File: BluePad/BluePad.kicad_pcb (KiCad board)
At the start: 2 copper layers, 76.2 x 95.2 mm, 213 parts, among them J1 USB_OTG, SW1 SW_RST, U1 ATMEGA32U4RC-A, U2 IS31FL3731, X1 16Mhz

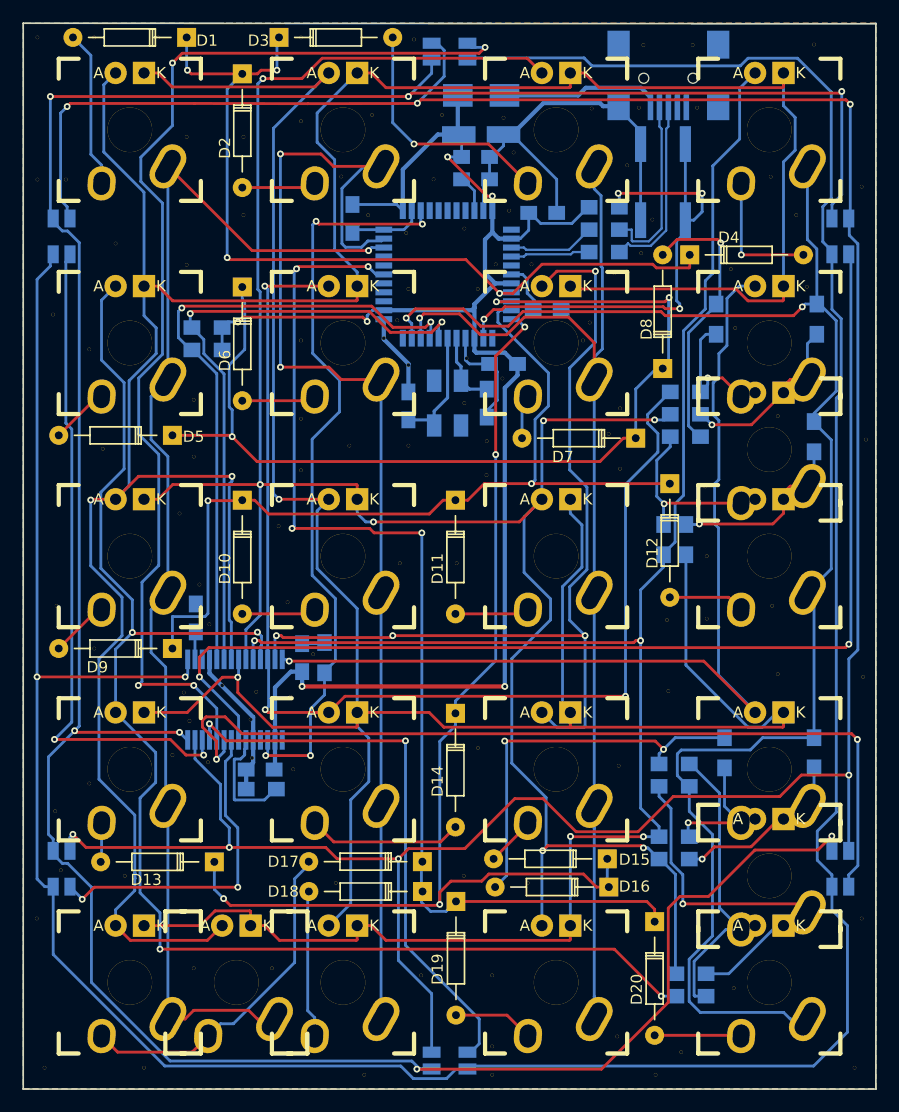
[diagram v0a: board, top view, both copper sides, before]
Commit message: Renamed BlueWeevil to LFK78
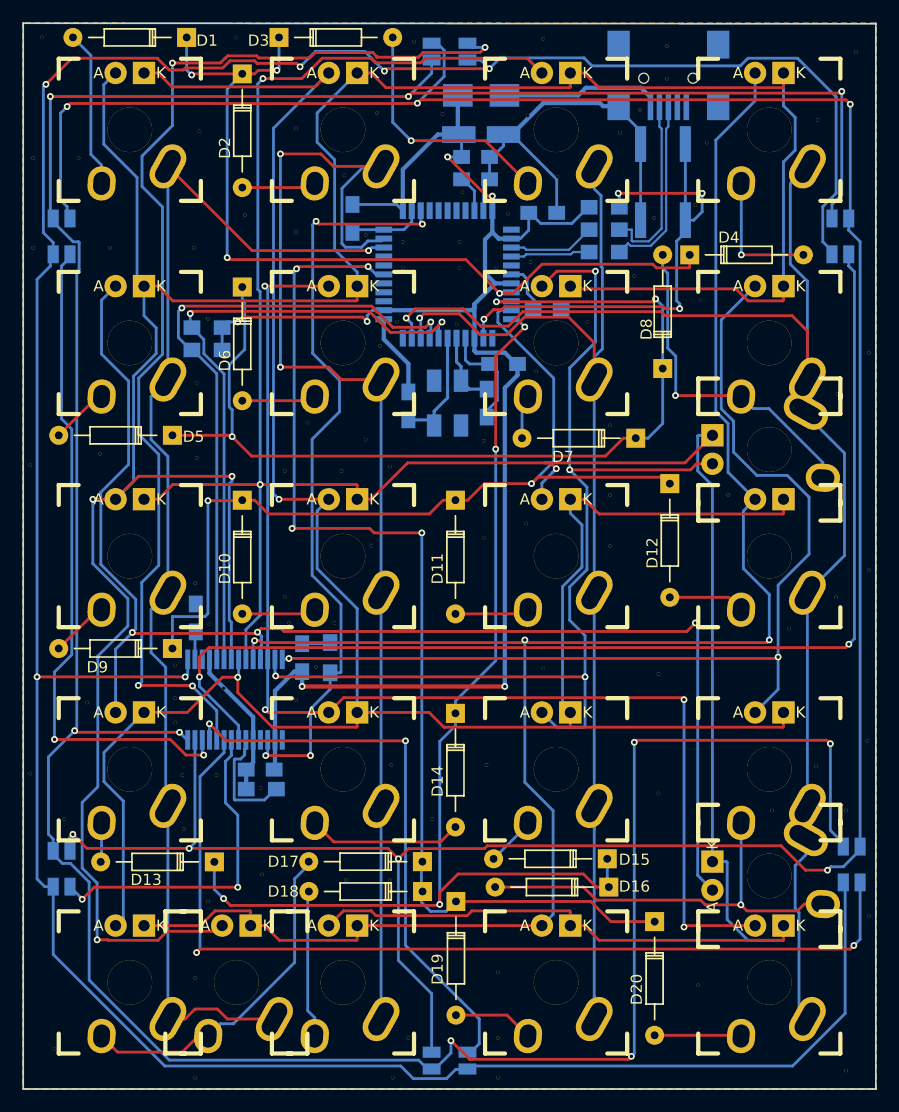
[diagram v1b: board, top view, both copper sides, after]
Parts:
- removed JP_ENTER_1, JP_ENTER_2, JP_ENTER_3, JP_ENTER_4, JP_PLUS_1, JP_PLUS_2, JP_PLUS_3, JP_PLUS_4: Jumper_NC_Small, Resistors_SMD:R_0805_HandSoldering
- removed JP_SW12_1, JP_SW12_2, JP_SW16_1, JP_SW16_2, JP_SW20_1, JP_SW20_2, JP_SW8_1, JP_SW8_2: Jumper_NO_Small, Resistors_SMD:R_0805_HandSoldering
- removed the REF** at (91.8, 41.0)
- removed the REF** at (34.5, 48.2)
- removed the REF** at (81.4, 41.4)
- removed the REF** at (72.4, 30.6)
- removed the REF** at (72.0, 35.8)
- removed the REF** at (60.8, 47.2)
- removed the REF** at (70.0, 56.4)
- removed the REF** at (68.0, 53.0)
- removed the REF** at (68.2, 49.0)
- removed the REF** at (71.4, 50.8)
- removed the REF** at (78.6, 47.4)
- removed the REF** at (69.2, 42.8)
- removed the REF** at (35.7, 57.1)
- removed the REF** at (63.0, 42.8)
- removed the REF** at (59.4, 36.2)
- removed the REF** at (62.8, 37.8)
- removed the REF** at (68.0, 37.4)
- removed the REF** at (79.2, 45.8)
- removed the REF** at (74.0, 40.6)
- removed the REF** at (63.0, 56.8)
- removed the REF** at (63.0, 49.6)
- removed the REF** at (53.4, 54.4)
- removed the REF** at (53.4, 59.0)
- removed the REF** at (31.2, 45.1)
- removed the REF** at (51.4, 64.0)
- removed the REF** at (52.2, 70.8)
- removed the REF** at (49.4, 78.8)
- removed the REF** at (42.9, 78.9)
- removed the REF** at (31.4, 89.5)
- removed the REF** at (81.8, 85.4)
- removed the REF** at (92.1, 105.3)
- removed the REF** at (87.4, 111.0)
- removed the REF** at (81.7, 109.6)
- removed the REF** at (98.6, 42.6)
- removed the REF** at (92.2, 46.3)
- removed the REF** at (95.4, 32.8)
- removed the REF** at (96.0, 54.2)
- removed the REF** at (89.5, 60.5)
- removed the REF** at (89.7, 66.7)
- removed the REF** at (89.7, 72.3)
- removed the REF** at (86.1, 72.4)
- removed the REF** at (95.5, 71.1)
- removed the REF** at (96.0, 77.2)
- removed the REF** at (86.2, 78.7)
- removed the REF** at (54.5, 75.4)
- removed the REF** at (52.5, 79.2)
- removed the REF** at (97.7, 36.2)
- removed the REF** at (45.2, 72.8)
- removed the REF** at (44.3, 69.2)
- removed the REF** at (49.0, 84.7)
- removed the REF** at (46.4, 78.2)
- removed the REF** at (43.4, 81.4)
- removed the REF** at (103.6, 77.5)
- removed the REF** at (103.9, 56.3)
- removed the REF** at (80.9, 55.8)
- removed the REF** at (81.9, 53.5)
- removed the REF** at (63.5, 20.5)
- removed the REF** at (43.8, 57.8)
- removed the REF** at (71.5, 27.5)
- removed the REF** at (65.2, 33.0)
- removed the REF** at (66.0, 27.2)
- removed the REF** at (57.0, 32.8)
- removed the REF** at (59.8, 27.2)
- removed the REF** at (82.5, 31.8)
- removed the REF** at (79.4, 26.7)
- removed the REF** at (53.4, 20.3)
- removed the REF** at (99.2, 21.0)
- removed the REF** at (103.5, 33.7)
- removed the REF** at (81.9, 58.9)
- removed the REF** at (103.5, 99.1)
- removed the REF** at (102.9, 112.4)
- removed the REF** at (85.1, 113.0)
- removed the REF** at (56.5, 95.9)
- removed the REF** at (50.8, 103.5)
- removed the REF** at (43.8, 103.5)
- removed the REF** at (48.9, 81.3)
- removed the REF** at (52.7, 85.7)
- removed the REF** at (41.9, 84.5)
- removed the REF** at (34.9, 74.9)
- removed the REF** at (70.0, 59.4)
- removed the REF** at (34.5, 87.0)
- removed the REF** at (37.7, 95.2)
- removed the REF** at (44.5, 90.8)
- removed the REF** at (45.1, 85.1)
- removed the REF** at (62.2, 67.3)
- removed the REF** at (67.3, 67.3)
- removed the REF** at (42.5, 62.9)
- removed the REF** at (43.8, 52.7)
- removed the REF** at (31.6, 71.1)
- removed the REF** at (36.8, 38.7)
- removed the REF** at (63.0, 60.3)
- removed the REF** at (48.3, 36.2)
- removed the REF** at (43.2, 40.6)
- removed the REF** at (48.3, 29.2)
- removed the REF** at (43.2, 29.2)
- removed the REF** at (40.6, 20.3)
- removed the REF** at (34.9, 20.3)
- removed the REF** at (32.4, 33.0)
- removed the REF** at (29.8, 33.0)
- removed the REF** at (29.8, 20.3)
- removed the REF** at (73.7, 95.9)
- removed the REF** at (31.9, 94.7)
- removed the REF** at (67.9, 95.2)
- removed the REF** at (69.2, 83.8)
- removed the REF** at (70.5, 104.1)
- removed the REF** at (64.1, 104.1)
- removed the REF** at (70.5, 110.5)
- removed the REF** at (70.5, 113.0)
- removed the REF** at (59.1, 113.0)
- removed the REF** at (39.4, 112.4)
- removed the REF** at (29.8, 99.1)
- removed the REF** at (30.5, 112.4)
- removed the REF** at (57.7, 56.8)
- removed the REF** at (88.8, 26.6)
- removed the REF** at (83.6, 26.6)
- removed the REF** at (88.4, 21.0)
- removed the REF** at (84.0, 21.0)
- removed the REF** at (53.4, 47.4)
- removed the REF** at (53.4, 27.8)
- removed the REF** at (62.0, 45.6)
- removed the REF** at (70.8, 40.6)
- removed the REF** at (84.8, 36.6)
- removed the REF** at (83.8, 39.6)
- added REF**: GND Via, Cherry:GNDVia, F.Cu at (44.1, 57.9)
- added REF**: GND Via, Cherry:GNDVia, F.Cu at (86.1, 24.0)
- added REF**: GND Via, Cherry:GNDVia, F.Cu at (53.0, 79.5)
- added REF**: GND Via, Cherry:GNDVia, F.Cu at (89.7, 29.7)
- added REF**: GND Via, Cherry:GNDVia, F.Cu at (88.6, 35.3)
- added REF**: GND Via, Cherry:GNDVia, F.Cu at (49.8, 87.4)
- added REF**: GND Via, Cherry:GNDVia, F.Cu at (46.5, 78.5)
- added REF**: GND Via, Cherry:GNDVia, F.Cu at (43.9, 69.1)
- added REF**: GND Via, Cherry:GNDVia, F.Cu at (79.0, 45.7)
- added REF**: GND Via, Cherry:GNDVia, F.Cu at (73.9, 40.4)
- added REF**: GND Via, Cherry:GNDVia, F.Cu at (70.9, 40.9)
- added REF**: GND Via, Cherry:GNDVia, F.Cu at (67.3, 46.0)
- added REF**: GND Via, Cherry:GNDVia, F.Cu at (73.7, 27.3)
- added REF**: GND Via, Cherry:GNDVia, F.Cu at (62.0, 45.7)
- added REF**: GND Via, Cherry:GNDVia, F.Cu at (67.6, 40.9)
- added REF**: GND Via, Cherry:GNDVia, F.Cu at (62.5, 40.9)
- added REF**: GND Via, Cherry:GNDVia, F.Cu at (86.1, 21.1)
- added REF**: GND Via, Cherry:GNDVia, F.Cu at (81.9, 28.8)
- added REF**: GND Via, Cherry:GNDVia, F.Cu at (85.0, 36.4)
- added REF**: GND Via, Cherry:GNDVia, F.Cu at (83.7, 26.8)
- added REF**: GND Via, Cherry:GNDVia, F.Cu at (76.3, 32.8)
- added REF**: GND Via, Cherry:GNDVia, F.Cu at (97.0, 73.2)
- added REF**: GND Via, Cherry:GNDVia, F.Cu at (91.6, 61.2)
- added REF**: GND Via, Cherry:GNDVia, F.Cu at (95.5, 89.4)
- added REF**: GND Via, Cherry:GNDVia, F.Cu at (99.4, 85.5)
- added REF**: GND Via, Cherry:GNDVia, F.Cu at (54.0, 54.7)
- added REF**: GND Via, Cherry:GNDVia, F.Cu at (102.1, 89.4)
- added REF**: GND Via, Cherry:GNDVia, F.Cu at (101.2, 70.4)
- added REF**: GND Via, Cherry:GNDVia, F.Cu at (45.1, 45.5)
- added REF**: GND Via, Cherry:GNDVia, F.Cu at (44.1, 51.2)
- added REF**: GND Via, Cherry:GNDVia, F.Cu at (42.9, 91.1)
- added REF**: GND Via, Cherry:GNDVia, F.Cu at (45.1, 97.5)
- added REF**: GND Via, Cherry:GNDVia, F.Cu at (49.9, 95.1)
- added REF**: GND Via, Cherry:GNDVia, F.Cu at (57.4, 95.6)
- added REF**: GND Via, Cherry:GNDVia, F.Cu at (65.2, 90.2)
- added REF**: GND Via, Cherry:GNDVia, F.Cu at (75.1, 76.7)
- added REF**: GND Via, Cherry:GNDVia, F.Cu at (51.9, 59.1)
- added REF**: GND Via, Cherry:GNDVia, F.Cu at (73.5, 63.8)
- added REF**: GND Via, Cherry:GNDVia, F.Cu at (74.4, 50.2)
- added REF**: GND Via, Cherry:GNDVia, F.Cu at (83.2, 41.7)
- added REF**: GND Via, Cherry:GNDVia, F.Cu at (89.0, 43.8)
- added REF**: GND Via, Cherry:GNDVia, F.Cu at (101.3, 52.2)
- added REF**: GND Via, Cherry:GNDVia, F.Cu at (99.6, 27.7)
- added REF**: GND Via, Cherry:GNDVia, F.Cu at (103.0, 21.6)
- added REF**: GND Via, Cherry:GNDVia, F.Cu at (104.1, 48.5)
- added REF**: GND Via, Cherry:GNDVia, F.Cu at (104.1, 67.9)
- added REF**: GND Via, Cherry:GNDVia, F.Cu at (85.3, 77.2)
- added REF**: GND Via, Cherry:GNDVia, F.Cu at (57.0, 59.1)
- added REF**: GND Via, Cherry:GNDVia, F.Cu at (85.3, 87.9)
- added REF**: GND Via, Cherry:GNDVia, F.Cu at (104.0, 83.2)
- added REF**: GND Via, Cherry:GNDVia, F.Cu at (104.1, 98.8)
- added REF**: GND Via, Cherry:GNDVia, F.Cu at (88.9, 105.0)
- added REF**: GND Via, Cherry:GNDVia, F.Cu at (102.1, 112.6)
- added REF**: GND Via, Cherry:GNDVia, F.Cu at (71.0, 103.9)
- added REF**: GND Via, Cherry:GNDVia, F.Cu at (70.0, 85.3)
- added REF**: GND Via, Cherry:GNDVia, F.Cu at (61.5, 85.3)
- added REF**: GND Via, Cherry:GNDVia, F.Cu at (61.3, 95.6)
- added REF**: GND Via, Cherry:GNDVia, F.Cu at (71.0, 109.7)
- added REF**: GND Via, Cherry:GNDVia, F.Cu at (61.3, 58.7)
- added REF**: GND Via, Cherry:GNDVia, F.Cu at (63.0, 109.7)
- added REF**: GND Via, Cherry:GNDVia, F.Cu at (61.6, 113.3)
- added REF**: GND Via, Cherry:GNDVia, F.Cu at (43.9, 113.3)
- added REF**: GND Via, Cherry:GNDVia, F.Cu at (43.9, 104.4)
- added REF**: GND Via, Cherry:GNDVia, F.Cu at (31.4, 110.7)
- added REF**: GND Via, Cherry:GNDVia, F.Cu at (32.3, 90.2)
- added REF**: GND Via, Cherry:GNDVia, F.Cu at (29.2, 86.1)
- added REF**: GND Via, Cherry:GNDVia, F.Cu at (34.3, 79.8)
- added REF**: GND Via, Cherry:GNDVia, F.Cu at (29.2, 58.5)
- added REF**: GND Via, Cherry:GNDVia, F.Cu at (35.4, 57.5)
- added REF**: GND Via, Cherry:GNDVia, F.Cu at (43.6, 111.1)
- added REF**: GND Via, Cherry:GNDVia, F.Cu at (29.5, 39.1)
- added REF**: GND Via, Cherry:GNDVia, F.Cu at (36.3, 39.1)
- added REF**: GND Via, Cherry:GNDVia, F.Cu at (33.5, 31.1)
- added REF**: GND Via, Cherry:GNDVia, F.Cu at (29.5, 31.1)
- added REF**: GND Via, Cherry:GNDVia, F.Cu at (43.8, 39.1)
- added REF**: GND Via, Cherry:GNDVia, F.Cu at (47.6, 20.3)
- added REF**: GND Via, Cherry:GNDVia, F.Cu at (30.2, 20.3)
- added REF**: GND Via, Cherry:GNDVia, F.Cu at (34.8, 20.3)
- added REF**: GND Via, Cherry:GNDVia, F.Cu at (58.8, 20.7)
- added REF**: GND Via, Cherry:GNDVia, F.Cu at (63.5, 20.7)
- added REF**: GND Via, Cherry:GNDVia, F.Cu at (71.0, 113.3)
- added REF**: GND Via, Cherry:GNDVia, F.Cu at (44.3, 28.7)
- added REF**: GND Via, Cherry:GNDVia, F.Cu at (48.4, 36.2)
- added REF**: GND Via, Cherry:GNDVia, F.Cu at (53.0, 28.4)
- added REF**: GND Via, Cherry:GNDVia, F.Cu at (53.0, 37.7)
- added REF**: GND Via, Cherry:GNDVia, F.Cu at (59.2, 38.0)
- added REF**: GND Via, Cherry:GNDVia, F.Cu at (67.6, 38.6)
- added REF**: GND Via, Cherry:GNDVia, F.Cu at (62.5, 38.6)
- added REF**: GND Via, Cherry:GNDVia, F.Cu at (60.5, 47.9)
- added REF**: GND Via, Cherry:GNDVia, F.Cu at (59.7, 65.8)
- added REF**: GND Via, Cherry:GNDVia, F.Cu at (59.2, 56.3)
- added REF**: GND Via, Cherry:GNDVia, F.Cu at (71.9, 36.1)
- added REF**: GND Via, Cherry:GNDVia, F.Cu at (69.7, 56.4)
- added REF**: GND Via, Cherry:GNDVia, F.Cu at (69.7, 65.0)
- added REF**: GND Via, Cherry:GNDVia, F.Cu at (81.0, 65.8)
- added REF**: GND Via, Cherry:GNDVia, F.Cu at (81.0, 61.2)
- added REF**: GND Via, Cherry:GNDVia, F.Cu at (81.0, 55.0)
- added REF**: GND Via, Cherry:GNDVia, F.Cu at (66.0, 27.2)
- added REF**: GND Via, Cherry:GNDVia, F.Cu at (60.2, 27.1)
- added REF**: GND Via, Cherry:GNDVia, F.Cu at (57.3, 32.6)
- added REF**: GND Via, Cherry:GNDVia, F.Cu at (67.8, 34.2)
- added REF**: GND Via, Cherry:GNDVia, F.Cu at (63.4, 34.0)
- added REF**: GND Via, Cherry:GNDVia, F.Cu at (75.1, 20.4)
- added REF**: GND Via, Cherry:GNDVia, F.Cu at (45.8, 86.2)
- added REF**: GND Via, Cherry:GNDVia, F.Cu at (42.8, 86.2)
- added REF**: GND Via, Cherry:GNDVia, F.Cu at (45.2, 72.8)
- added REF**: GND Via, Cherry:GNDVia, F.Cu at (42.2, 76.5)
- added REF**: GND Via, Cherry:GNDVia, F.Cu at (42.2, 79.4)
- added REF**: GND Via, Cherry:GNDVia, F.Cu at (42.2, 81.5)
- added REF**: GND Via, Cherry:GNDVia, F.Cu at (52.3, 72.6)
- added REF**: GND Via, Cherry:GNDVia, F.Cu at (51.9, 70.4)
- added REF**: GND Via, Cherry:GNDVia, F.Cu at (56.4, 72.6)
- added REF**: GND Via, Cherry:GNDVia, F.Cu at (54.7, 76.6)
- moved RGB10 1.09 mm to (102.6, 94.2)
- moved R9 0.51 mm to (56.0, 75.8)
- turned SW_2U_ENTER_1 to 270 degrees
- turned SW_2U_PLUS_1 to 270 degrees
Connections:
- J1 pad 4: (no net) -> Net-(J1-Pad4)
- SW_12 pad A: NET_PLUS_SW2 -> CA4
- SW_12 pad K: NET_PLUS_SW1 -> CA2
- SW_16 pad SW1: NET_SW16_1 -> C4
- SW_16 pad SW2: NET_SW16_2 -> Net-(D16-Pad2)
- SW_17 pad A: CA1 -> CA2
- SW_18 pad A: CA2 -> CA3
- SW_19 pad A: CA3 -> CA4
- SW_19 pad K: CA4 -> CA3
- SW_20 pad A: NET_ENTER_SW2 -> CA6
- SW_20 pad K: NET_ENTER_SW1 -> CA3
- SW_2U_ENTER_1 pad A: NET_SW16_2 -> CA5
- SW_2U_ENTER_1 pad K: NET_SW16_1 -> CA3
- SW_2U_ENTER_1 pad SW1: NET_ENTER_SW1 -> C4
- SW_2U_ENTER_1 pad SW2: NET_ENTER_SW2 -> Net-(D16-Pad2)
- SW_2U_PLUS_1 pad A: NET_SW8_2 -> CA7
- SW_2U_PLUS_1 pad K: NET_SW8_1 -> CA3
- SW_2U_PLUS_1 pad SW1: NET_PLUS_SW1 -> C4
- SW_2U_PLUS_1 pad SW2: NET_PLUS_SW2 -> Net-(D8-Pad2)
- SW_8 pad SW1: NET_SW8_1 -> C4
- SW_8 pad SW2: NET_SW8_2 -> Net-(D8-Pad2)
- U1 pad 1: (no net) -> Net-(U1-Pad1)
- U1 pad 12: (no net) -> Net-(U1-Pad12)
- U1 pad 22: (no net) -> Net-(U1-Pad22)
- U1 pad 25: (no net) -> Net-(U1-Pad25)
- U1 pad 26: (no net) -> Net-(U1-Pad26)
- U1 pad 27: (no net) -> Net-(U1-Pad27)
- U1 pad 29: (no net) -> Net-(U1-Pad29)
- U1 pad 30: (no net) -> Net-(U1-Pad30)
- U1 pad 37: (no net) -> Net-(U1-Pad37)
- U1 pad 38: (no net) -> Net-(U1-Pad38)
- U1 pad 39: (no net) -> Net-(U1-Pad39)
- U1 pad 40: (no net) -> Net-(U1-Pad40)
- U1 pad 41: (no net) -> Net-(U1-Pad41)
- U2 pad 1: (no net) -> CA9
- U2 pad 17: (no net) -> Net-(U2-Pad17)
- U2 pad 4: (no net) -> Net-(U2-Pad4)
- X1 pad 3: (no net) -> GND
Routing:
- net CA3: track 202.0 -> 237.5 mm, vias 7 -> 3
- net NET_ENTER_SW1: track 34.3 -> 0.00 mm, vias 1 -> 0
- net NET_ENTER_SW2: track 26.3 -> 0.00 mm
- net CB8: track 266.9 -> 290.8 mm, vias 7 -> 9
- net C4: track 144.1 -> 126.3 mm, vias 2 -> 1
- net NET_SW16_1: track 16.7 -> 0.00 mm, vias 1 -> 0
- net NET_PLUS_SW1: track 16.7 -> 0.00 mm, vias 1 -> 0
- net NET_PLUS_SW2: track 16.6 -> 0.00 mm, vias 1 -> 0
- net NET_SW8_1: track 16.4 -> 0.00 mm, vias 1 -> 0
- net NET_SW8_2: track 12.8 -> 0.00 mm, vias 1 -> 0
- net CA7: track 83.2 -> 95.4 mm
- net NET_SW16_2: track 11.6 -> 0.00 mm, vias 1 -> 0
- net CA5: track 127.8 -> 120.8 mm, vias 4 -> 3
- net CB3: track 79.0 -> 84.9 mm
- net Net-(D8-Pad2): track 24.7 -> 30.1 mm
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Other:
- board text removed: "JP-ENTER"
- board text removed: "JP-PLUS"
- board text removed: "JP-SW12"
- board text removed: "JP-SW16"
- board text removed: "JP-SW20"
- board text removed: "JP-SW8"
